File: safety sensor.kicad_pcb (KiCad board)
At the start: 2 copper layers, 48.3 x 35.6 mm, 14 parts, among them J1 Conn_01x05, U1 VCNL3020-GS08

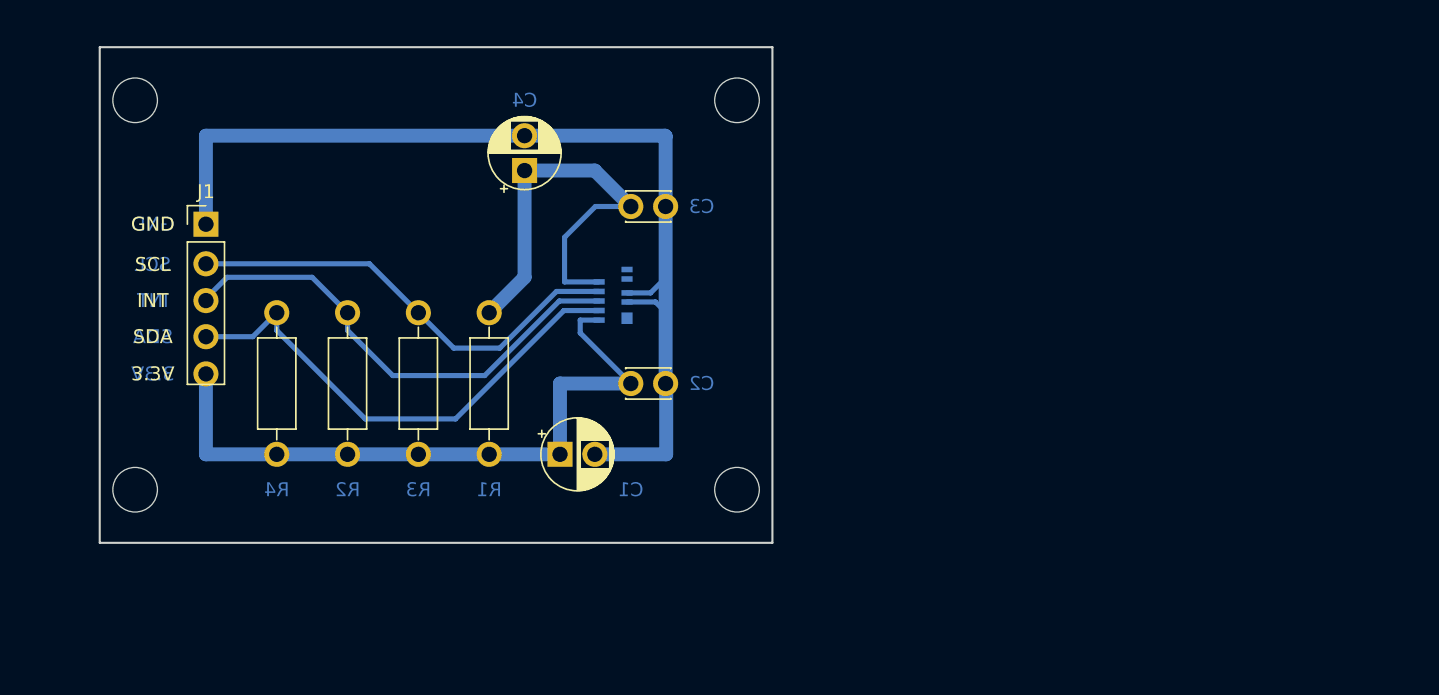
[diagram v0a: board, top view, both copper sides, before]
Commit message: add stm8 to the board with connection to interrupt line of vcnl3020
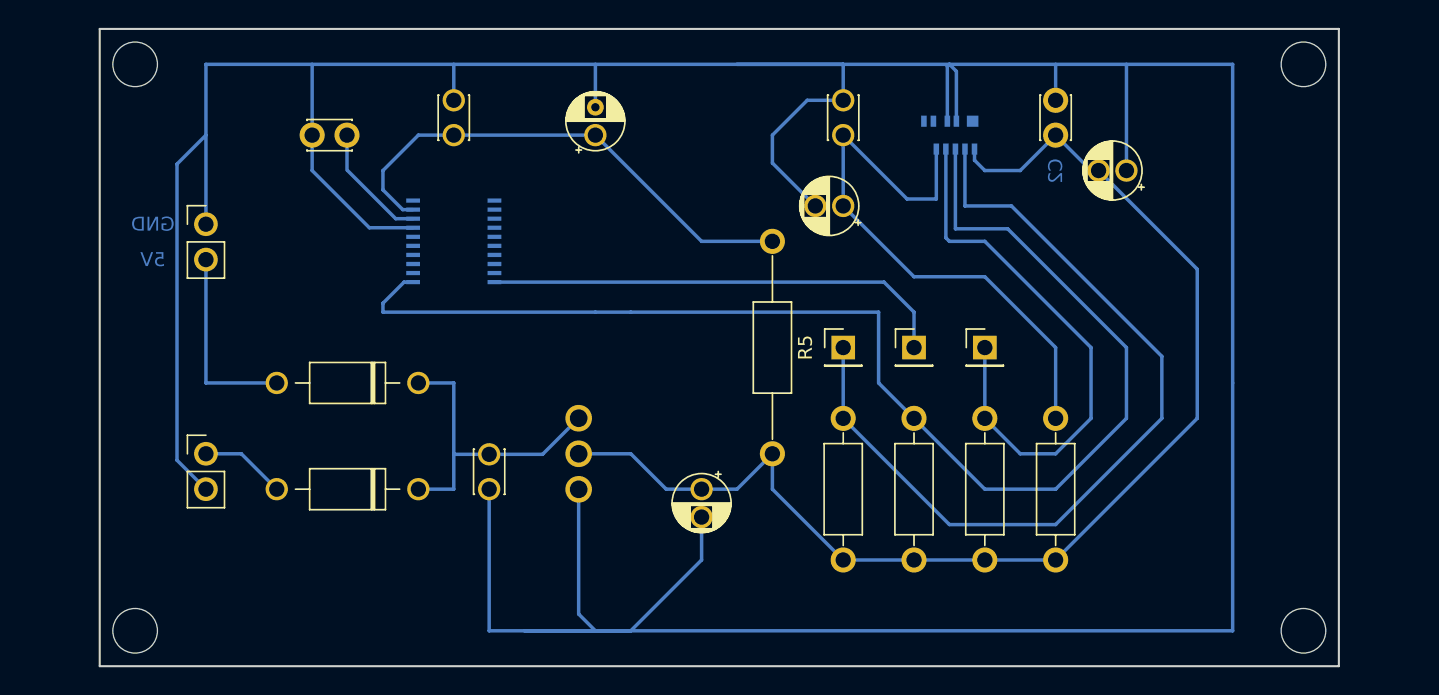
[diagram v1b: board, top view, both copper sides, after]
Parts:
- added C5: 100nF, Capacitor_THT:C_Disc_D3.0mm_W2.0mm_P2.50mm, F.Cu at (50.8, 50.8)
- added C6: 10uF, Capacitor_THT:CP_Radial_D4.0mm_P2.00mm, F.Cu at (66.0, 50.8)
- added C7: 100nF, Capacitor_THT:C_Disc_D3.0mm_W2.0mm_P2.50mm, F.Cu at (48.3, 25.4)
- added C8: 100nF, Capacitor_THT:C_Disc_D3.0mm_W2.0mm_P2.50mm, F.Cu at (76.2, 25.4)
- added C9: 10uF, Capacitor_THT:CP_Radial_D4.0mm_P2.00mm, F.Cu at (76.2, 30.5)
- added D1: 1N5817, Diode_THT:D_DO-41_SOD81_P10.16mm_Horizontal, F.Cu at (45.7, 43.2)
- added D2: 1N5817, Diode_THT:D_DO-41_SOD81_P10.16mm_Horizontal, F.Cu at (45.7, 50.8)
- added IC1: STM8S003F3P6, safety sensor:TSSOP20, B.Cu at (48.3, 33.0)
- added J2: Conn_01x01, Connector_PinHeader_2.54mm:PinHeader_1x01_P2.54mm_Vertical, F.Cu at (76.2, 40.6)
- added J3: Conn_01x01, Connector_PinHeader_2.54mm:PinHeader_1x01_P2.54mm_Vertical, F.Cu at (86.4, 40.6)
- added J4: Conn_01x01, Connector_PinHeader_2.54mm:PinHeader_1x01_P2.54mm_Vertical, F.Cu at (81.3, 40.6)
- added J5: Conn_01x02, Connector_PinHeader_2.54mm:PinHeader_1x02_P2.54mm_Vertical, F.Cu at (30.5, 48.3)
- added R5: 0, Resistor_THT:R_Axial_DIN0207_L6.3mm_D2.5mm_P15.24mm_Horizontal, F.Cu at (71.1, 33.0)
- added U2: VCNL3020-GS08, safety sensor:XDCR_VCNL3020-GS08, B.Cu at (83.8, 25.4)
- C1: footprint Capacitor_THT:CP_Radial_D5.0mm_P2.50mm -> Capacitor_THT:CP_Radial_D4.0mm_P2.00mm
- C4: value 10uF -> 1uF; footprint Capacitor_THT:CP_Radial_D5.0mm_P2.50mm -> Capacitor_THT:CP_Radial_D4.0mm_P2.00mm
- J1: value Conn_01x05 -> Conn_01x02; footprint Connector_PinHeader_2.54mm:PinHeader_1x05_P2.54mm_Vertical -> Connector_PinHeader_2.54mm:PinHeader_1x02_P2.54mm_Vertical
- R1: value 10 -> 10K
- R2: value 10K -> 4.7K
- R4: value 4.7K -> 10
- U1: value VCNL3020-GS08 -> LD1117V33; footprint aaaaaaaaaaaaaaa:XDCR_VCNL3020-GS08 -> safety sensor:TO255P1020X450X1968-3
- moved R4 56.4 mm to (91.4, 55.9)
- moved C1 45.5 mm to (96.5, 27.9), turned to 180 degrees
- moved REF** 41.9 mm to (109.2, 61.0)
- moved R3 41.3 mm to (86.4, 55.9)
- moved REF** 40.7 mm to (109.2, 20.3)
- moved R2 39.7 mm to (76.2, 55.9), turned to 90 degrees
- moved C2 36.6 mm to (91.4, 22.9), turned to -90 degrees
- moved R1 30.6 mm to (81.3, 45.7), turned to -90 degrees
- moved C3 23.4 mm to (38.1, 25.4)
- moved U1 11.5 mm to (57.8, 48.3), turned to 90 degrees
- moved REF** 10.1 mm to (25.4, 61.0)
- moved C4 5.68 mm to (58.4, 25.4)
- moved REF** 2.58 mm to (25.4, 20.3)
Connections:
- C1 pad 1: (no net) -> GND
- C1 pad 2: (no net) -> +3.3V
- C2 pad 1: (no net) -> GND
- C2 pad 2: (no net) -> +3.3V
- C3 pad 1: (no net) -> GND
- C3 pad 2: (no net) -> Net-(C3-Pad2)
- C4 pad 1: (no net) -> +3.3V
- C4 pad 2: (no net) -> GND
- J1 pad 1: (no net) -> GND
- J1 pad 2: (no net) -> +5V
- R1 pad 1: (no net) -> Net-(IC1-Pad1)
- R1 pad 2: (no net) -> +3.3V
- R2 pad 1: (no net) -> +3.3V
- R2 pad 2: (no net) -> Net-(J2-Pad1)
- R3 pad 1: (no net) -> +3.3V
- R3 pad 2: (no net) -> Net-(J3-Pad1)
- R4 pad 1: (no net) -> +3.3V
- R4 pad 2: (no net) -> Net-(C8-Pad1)
- U1 pad 1: (no net) -> GND
- U1 pad 2: (no net) -> +3.3V
- U1 pad 3: (no net) -> Net-(C5-Pad2)
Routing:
- net GND: track 0.00 -> 308.4 mm
- net (no net): track 257.1 -> 0.00 mm
- net +3.3V: track 0.00 -> 124.4 mm
- net Net-(IC1-Pad1): track 0.00 -> 93.7 mm
- net Net-(J2-Pad1): track 0.00 -> 61.4 mm
- net Net-(C8-Pad1): track 0.00 -> 41.8 mm
- net Net-(J3-Pad1): track 0.00 -> 39.9 mm
- net Net-(IC1-Pad20): track 0.00 -> 33.5 mm
- net Net-(C5-Pad2): track 0.00 -> 22.7 mm
- net +5V: track 0.00 -> 13.9 mm
- net Net-(C3-Pad2): track 0.00 -> 8.63 mm
- net +4V: track 0.00 -> 6.13 mm
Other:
- board size 48.3 x 35.6 mm -> 88.9 x 45.7 mm
- board text added: "5V"
- board text removed: "3.3V"
- board text removed: "INT"
- board text removed: "SCL"
- board text removed: "SDA"

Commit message: increase track width and pad size change
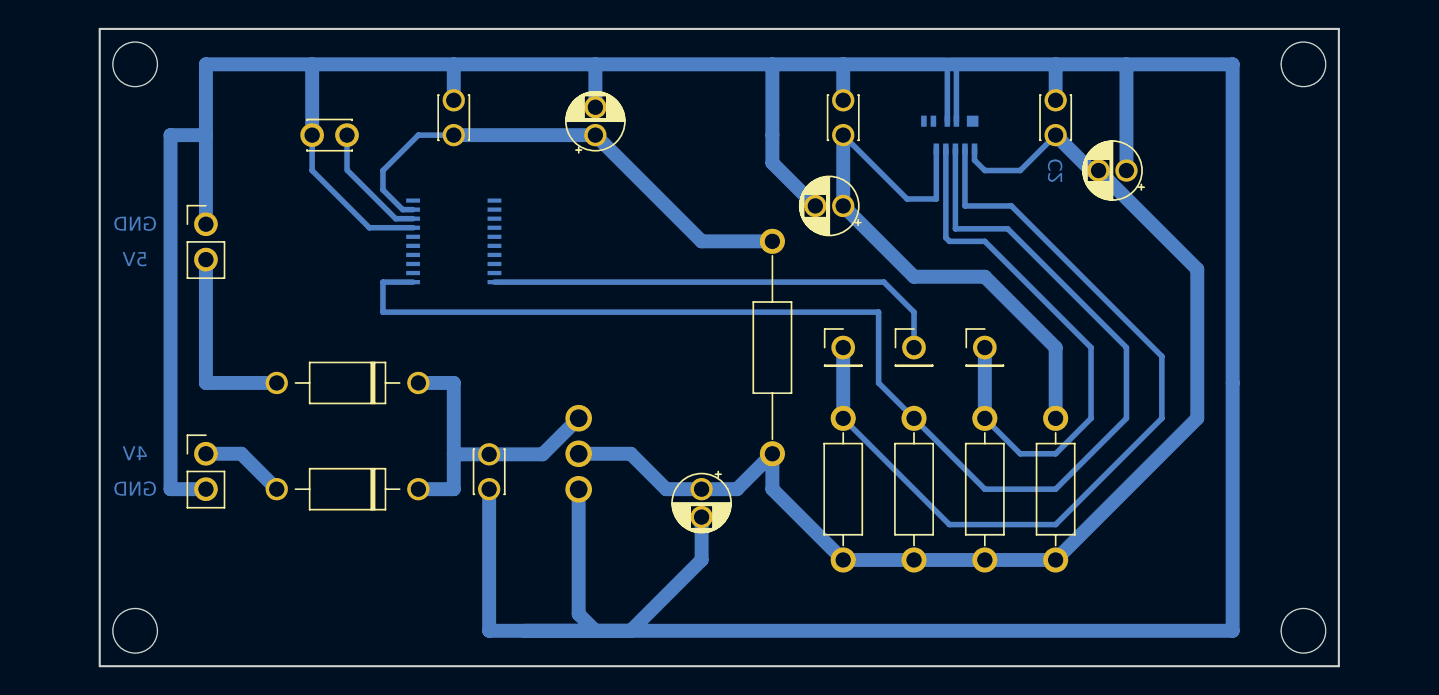
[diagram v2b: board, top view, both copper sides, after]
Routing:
- net GND: track 308.4 -> 303.1 mm
- net Net-(IC1-Pad1): track 93.7 -> 94.6 mm
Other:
- board text added: "4V"

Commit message: add SWIM connector
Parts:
- added J6: Conn_01x01, Connector_PinHeader_2.54mm:PinHeader_1x01_P2.54mm_Vertical, F.Cu at (58.4, 30.5)
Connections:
- IC1 pad 18: unconnected-(IC1-Pad18) -> Net-(IC1-Pad18)
- J5 pad 1: +4V -> Net-(J5-Pad1)
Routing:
- net Net-(IC1-Pad18): track 0.00 -> 10.5 mm
- net Net-(J5-Pad1): track 0.00 -> 6.13 mm
- net +4V: track 6.13 -> 0.00 mm
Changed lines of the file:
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@@
   (net 16 "unconnected-(IC1-Pad16)")
   (net 17 "unconnected-(IC1-Pad17)")
-  (net 18 "unconnected-(IC1-Pad18)")
+  (net 18 "Net-(IC1-Pad18)")
   (net 19 "unconnected-(IC1-Pad19)")
   (net 20 "unconnected-(U2-Pad10)")
@@
   (net 28 "Net-(IC1-Pad20)")
   (net 29 "Net-(IC1-Pad1)")
+  (net 30 "Net-(J5-Pad1)")
   (footprint "Connector_PinHeader_2.54mm:PinHeader_1x01_P2.54mm_Vertical" (layer "F.Cu")
     (at 86.36 40.64)
@@
     )
   )
+  (footprint "Connector_PinHeader_2.54mm:PinHeader_1x01_P2.54mm_Vertical" (layer "F.Cu")
+    (at 58.42 30.48)
+    (descr "Through hole straight pin header, 1x01, 2.54mm pitch, single row")
+    (tags "Through hole pin header THT 1x01 2.54mm single row")
+    (property "Sheetfile" "safety sensor.kicad_sch")
+    (property "Sheetname" "")
+    (attr through_hole)
+    (fp_text reference "J6" (at 0 -2.33) (layer "F.SilkS") hide
+      (effects (font (size 1 1) (thickness 0.15)))
+    )
+    (fp_text value "Conn_01x01" (at 0 2.33) (layer "F.Fab")
+      (effects (font (size 1 1) (thickness 0.15)))
+    )
+    (fp_text user "${REFERENCE}" (at 0 0 90) (layer "F.Fab")
+      (effects (font (size 1 1) (thickness 0.15)))
+    )
+    (fp_line (start -1.33 1.33) (end 1.33 1.33) (layer "F.SilkS") (width 0.12))
+    (fp_line (start -1.33 1.27) (end -1.33 1.33) (layer "F.SilkS") (width 0.12))
+    (fp_line (start -1.33 -1.33) (end 0 -1.33) (layer "F.SilkS") (width 0.12))
+    (fp_line (start -1.33 1.27) (end 1.33 1.27) (layer "F.SilkS") (width 0.12))
+    (fp_line (start -1.33 0) (end -1.33 -1.33) (layer "F.SilkS") (width 0.12))
+    (fp_line (start 1.33 1.27) (end 1.33 1.33) (layer "F.SilkS") (width 0.12))
+    (fp_line (start -1.8 -1.8) (end -1.8 1.8) (layer "F.CrtYd") (width 0.05))
+    (fp_line (start -1.8 1.8) (end 1.8 1.8) (layer "F.CrtYd") (width 0.05))
+    (fp_line (start 1.8 1.8) (end 1.8 -1.8) (layer "F.CrtYd") (width 0.05))
+    (fp_line (start 1.8 -1.8) (end -1.8 -1.8) (layer "F.CrtYd") (width 0.05))
+    (fp_line (start 1.27 -1.27) (end 1.27 1.27) (layer "F.Fab") (width 0.1))
+    (fp_line (start 1.27 1.27) (end -1.27 1.27) (layer "F.Fab") (width 0.1))
+    (fp_line (start -1.27 -0.635) (end -0.635 -1.27) (layer "F.Fab") (width 0.1))
+    (fp_line (start -0.635 -1.27) (end 1.27 -1.27) (layer "F.Fab") (width 0.1))
+    (fp_line (start -1.27 1.27) (end -1.27 -0.635) (layer "F.Fab") (width 0.1))
+    (pad "1" thru_hole circle (at 0 0) (size 1.7 1.7) (drill 1.1) (layers *.Cu *.Mask)
+      (net 18 "Net-(IC1-Pad18)") (pinfunction "Pin_1") (pintype "passive"))
+    (model "${KICAD6_3DMODEL_DIR}/Connector_PinHeader_2.54mm.3dshapes/PinHeader_1x01_P2.54mm_Vertical.wrl"
+      (offset (xyz 0 0 0))
+      (scale (xyz 1 1 1))
+      (rotate (xyz 0 0 0))
+    )
+  )
   (footprint "MountingHole:MountingHole_3.2mm_M3" (layer "F.Cu")
     (at 109.22 60.96)
@@
     (fp_line (start -1.27 3.81) (end -1.27 -0.635) (layer "F.Fab") (width 0.1))
     (pad "1" thru_hole oval (at 0 0) (size 1.7 1.7) (drill 1.1) (layers *.Cu *.Mask)
-      (net 24 "+4V") (pinfunction "Pin_1") (pintype "passive"))
+      (net 30 "Net-(J5-Pad1)") (pinfunction "Pin_1") (pintype "passive"))
     (pad "2" thru_hole oval (at 0 2.54) (size 1.7 1.7) (drill 1.1) (layers *.Cu *.Mask)
       (net 2 "GND") (pinfunction "Pin_2") (pintype "passive"))
@@
       (net 17 "unconnected-(IC1-Pad17)") (pinfunction "PC7(HS)/SPI_MISO[TIM1_CH2]") (pintype "bidirectional"))
     (pad "18" smd rect locked (at -1.625 2.9178 90) (size 0.3048 0.9906) (layers "B.Cu" "B.Paste" "B.Mask")
-      (net 18 "unconnected-(IC1-Pad18)") (pinfunction "PD1(HS)/SWIM") (pintype "bidirectional"))
+      (net 18 "Net-(IC1-Pad18)") (pinfunction "PD1(HS)/SWIM") (pintype "bidirectional"))
     (pad "19" smd rect locked (at -2.275 2.9178 90) (size 0.3048 0.9906) (layers "B.Cu" "B.Paste" "B.Mask")
       (net 19 "unconnected-(IC1-Pad19)") (pinfunction "PD2(HS)/AIN3/[TIM2_CH3]") (pintype "bidirectional"))
@@
   (segment (start 91.44 40.64) (end 86.36 35.56) (width 1) (layer "B.Cu") (net 4))
   (segment (start 76.2 30.48) (end 76.2 25.4) (width 1) (layer "B.Cu") (net 4))
+  (segment (start 55.88 33.02) (end 55.88 30.48) (width 0.4) (layer "B.Cu") (net 18))
+  (segment (start 55.88 30.48) (end 58.42 30.48) (width 0.4) (layer "B.Cu") (net 18))
+  (segment (start 51.1778 34.645) (end 54.255 34.645) (width 0.4) (layer "B.Cu") (net 18))
+  (segment (start 54.255 34.645) (end 55.88 33.02) (width 0.4) (layer "B.Cu") (net 18))
   (segment (start 48.26 48.26) (end 48.3 48.3) (width 0.25) (layer "B.Cu") (net 23))
   (segment (start 54.63 48.3) (end 57.22 45.71) (width 1) (layer "B.Cu") (net 23))
@@
   (segment (start 48.26 43.18) (end 48.26 48.26) (width 1) (layer "B.Cu") (net 23))
   (segment (start 45.72 43.18) (end 48.26 43.18) (width 1) (layer "B.Cu") (net 23))
-  (segment (start 33.02 48.26) (end 35.56 50.8) (width 1) (layer "B.Cu") (net 24))
-  (segment (start 30.48 48.26) (end 33.02 48.26) (width 1) (layer "B.Cu") (net 24))
   (segment (start 30.48 43.18) (end 35.56 43.18) (width 1) (layer "B.Cu") (net 25))
   (segment (start 30.48 34.33) (end 30.48 43.18) (width 1) (layer "B.Cu") (net 25))
@@
   (segment (start 86.36 50.8) (end 81.28 45.72) (width 0.4) (layer "B.Cu") (net 29))
   (segment (start 96.52 45.72) (end 91.44 50.8) (width 0.4) (layer "B.Cu") (net 29))
+  (segment (start 33.02 48.26) (end 35.56 50.8) (width 1) (layer "B.Cu") (net 30))
+  (segment (start 30.48 48.26) (end 33.02 48.26) (width 1) (layer "B.Cu") (net 30))
 )

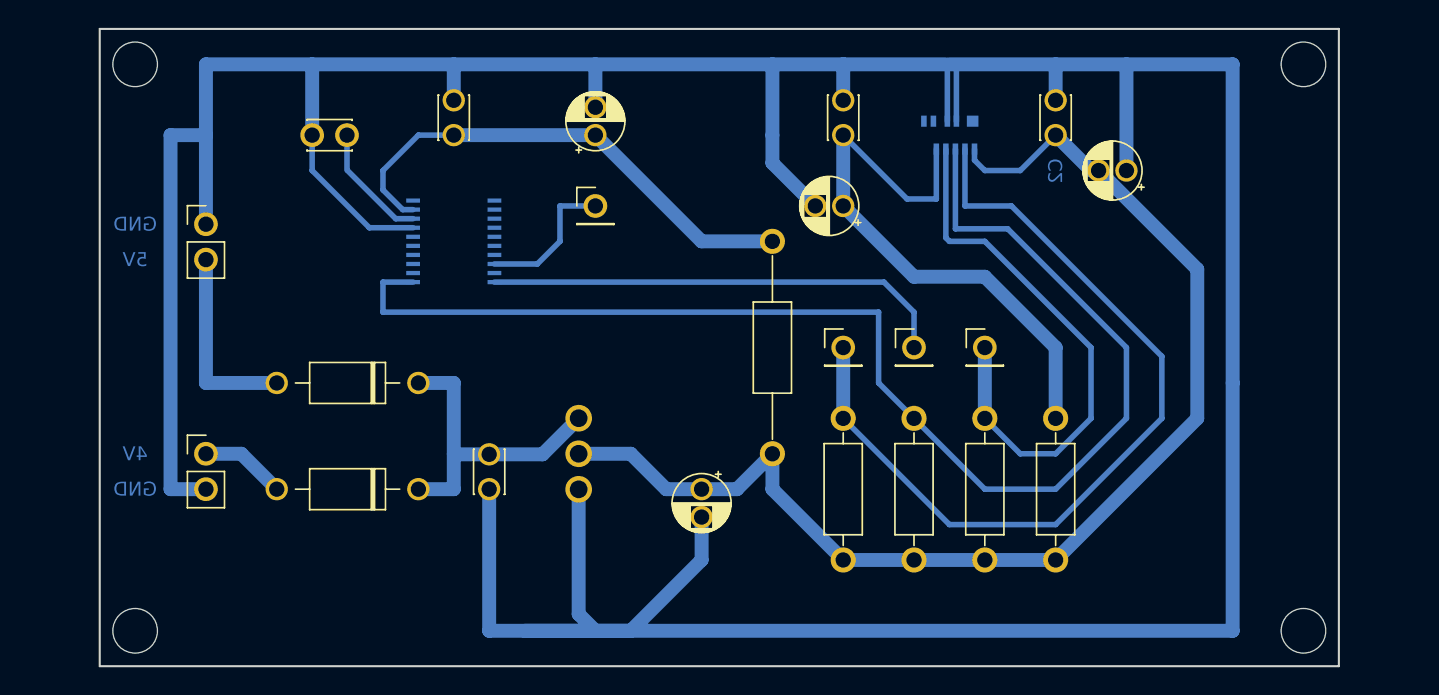
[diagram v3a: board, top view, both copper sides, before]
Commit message: polish schematics, add leds for voltage lines and gpio for stm8
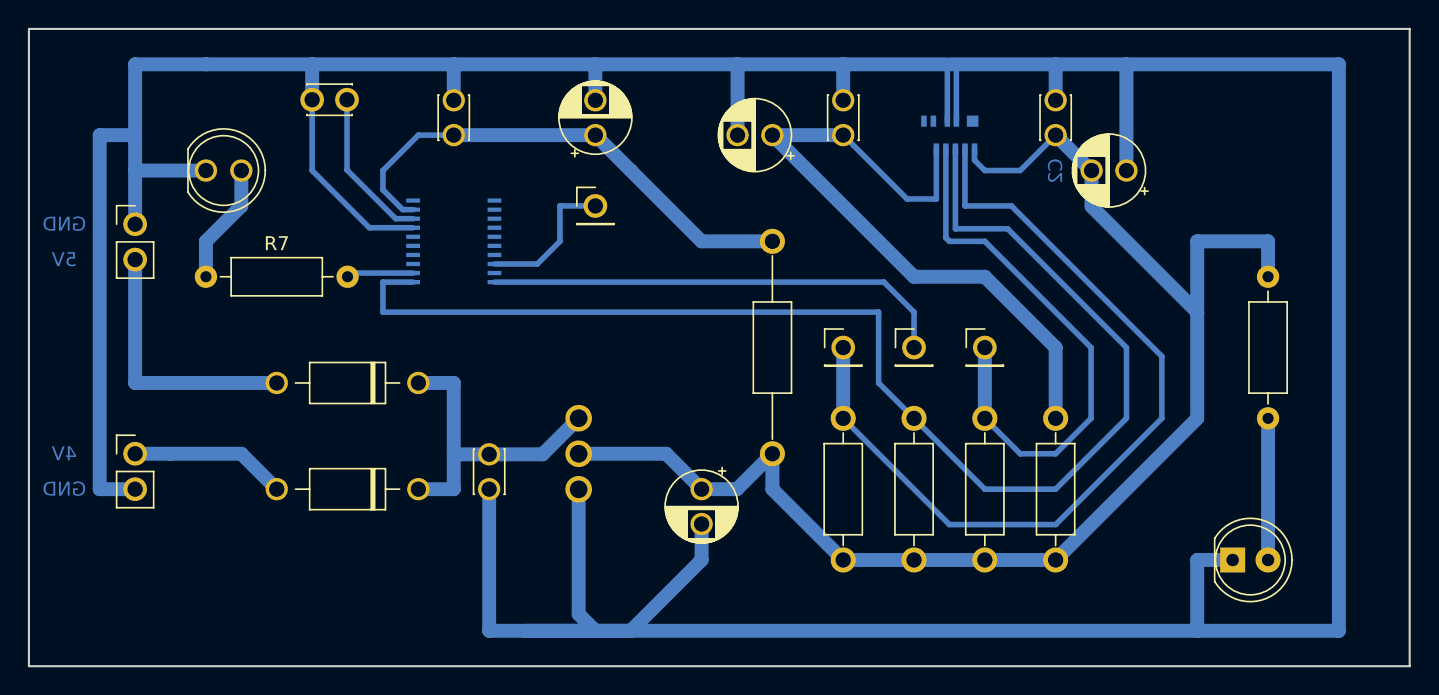
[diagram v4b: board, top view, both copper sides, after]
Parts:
- removed REF** (x4): MountingHole_3.2mm_M3, MountingHole:MountingHole_3.2mm_M3
- added D3: LED, LED_THT:LED_D5.0mm, F.Cu at (104.1, 55.9)
- added D4: LED, LED_THT:LED_D5.0mm, F.Cu at (30.5, 27.9)
- added R6: 1k, Resistor_THT:R_Axial_DIN0207_L6.3mm_D2.5mm_P10.16mm_Horizontal, F.Cu at (106.7, 45.7)
- added R7: 1k, Resistor_THT:R_Axial_DIN0207_L6.3mm_D2.5mm_P10.16mm_Horizontal, F.Cu at (30.5, 35.6)
- C1, C4, C6, C9: footprint Capacitor_THT:CP_Radial_D4.0mm_P2.00mm -> Capacitor_THT:CP_Radial_D5.0mm_P2.50mm
- moved C9 7.18 mm to (71.1, 25.4)
- moved J1 5.08 mm to (25.4, 31.8)
- moved J5 5.08 mm to (25.4, 48.3)
- moved C3 2.54 mm to (38.1, 22.9)
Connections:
- IC1 pad 2: unconnected-(IC1-Pad2) -> Net-(IC1-Pad2)
- J5 pad 1: Net-(J5-Pad1) -> +4V
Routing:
- net GND: track 303.1 -> 328.7 mm
- net +3.3V: track 124.4 -> 136.9 mm
- net +4V: track 0.00 -> 11.2 mm
- net Net-(D3-Pad2): track 0.00 -> 10.2 mm
- net Net-(D4-Pad2): track 0.00 -> 8.67 mm
- net Net-(C8-Pad1): track 41.8 -> 49.0 mm
- net Net-(J5-Pad1): track 6.13 -> 0.00 mm
- net +5V: track 13.9 -> 19.0 mm
- net Net-(IC1-Pad2): track 0.00 -> 4.81 mm
- net Net-(C3-Pad2): track 8.63 -> 11.2 mm
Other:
- board size 88.9 x 45.7 mm -> 99.1 x 45.7 mm
